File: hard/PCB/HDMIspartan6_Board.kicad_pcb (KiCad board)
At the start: 4 copper layers, 56.1 x 89.6 mm, 150 parts, among them IC1 W9812G6KH, P1 CONN_02X20, P2 CONN_01X03, U1 XC6SLX9-2TQG144C, U2 TPS62133RGTR, U3 ZLDO1117G33TA, U4 ZLDO1117G12TA, U5 MAX5864

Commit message: Add jmp Rpi Power
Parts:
- added P3: CONN_01X03, Pin_Headers:Pin_Header_Straight_1x03_Pitch2.54mm, F.Cu at (125.4, 115.0)
- added TH21, TH27, TH33, TH39: CONN_1, Project:1Pin_12mil_VIA, F.Cu at (136.3, 159.3)
- C10: value 3.3nF -> 33uF
- C4: value 33uF -> 3.3nF
- C5, C8: value 100n -> 33uF
- C6, C9: value 33uF -> 100n
- CA1, CA2, CA3, RF2, RF3: moved to F.Cu
- moved RF1 36.6 mm to (181.0, 147.4)
- moved RF4 34.7 mm to (177.4, 146.5)
- moved CF4 27.1 mm to (177.7, 142.4)
- moved CF1 26.4 mm to (177.6, 130.8)
- moved LF1 20.1 mm to (181.9, 139.7)
- moved CF3 16.9 mm to (177.7, 138.1), turned to 0 degrees
- moved RF6 16.7 mm to (182.2, 130.7), turned to 0 degrees
- moved CF6 15.1 mm to (187.3, 141.8)
- moved CF2 13.0 mm to (186.6, 130.9)
- moved CF5 12.8 mm to (182.2, 135.8), turned to 0 degrees
- moved CA2 12.7 mm to (168.7, 69.1), turned to 180 degrees
- moved CA3 11.4 mm to (168.8, 71.5), turned to 0 degrees
- moved CA1 10.9 mm to (168.6, 74.0), turned to 180 degrees
- moved PA1 10.7 mm to (162.1, 78.5), turned to 180 degrees
- moved DS2 9.36 mm to (95.1, 112.3)
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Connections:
- C10 pad 1: Net-(C10-Pad1) -> +1V2
- C4 pad 1: +5V -> Net-(C4-Pad1)
- C5 pad 1: +3V3 -> +5V
- C8 pad 1: +1V2 -> +3V3
- P1 pad 10: /spartan6/RXD -> /spartan6/TXD
- P1 pad 17: +3V3 -> Net-(P1-Pad17)
- P1 pad 2: VDD5V -> VccRpi
- P1 pad 4: VDD5V -> VccRpi
- P1 pad 8: /spartan6/TXD -> /spartan6/RXD
- U2 pad 9: Net-(C10-Pad1) -> Net-(C4-Pad1)
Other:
- board text added: "Convenciones referencias componentes: > H: HDMI. Ej.: RH1 > S: Spartan. Ej.: CS1 > A: ADC. Ej.: CA1 > F: FTDI. Ej.: RF2"

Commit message: config power
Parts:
- removed P2: CONN_01X03, Socket_Strips:Socket_Strip_Straight_1x03_Pitch2.54mm
- removed TH51, TH52, TH53, TH54: CONN_1, Project:1Pin_12mil_VIA
- C10, C5, C8: footprint Capacitors_SMD:C_0603 -> Capacitors_SMD:C_1206
- C4: footprint Capacitors_SMD:C_1206 -> Capacitors_SMD:C_0603; moved to F.Cu
- C6, C9: footprint Capacitors_SMD:C_1206 -> Capacitors_SMD:C_0603
- F1: moved to F.Cu
- P3: footprint Pin_Headers:Pin_Header_Straight_1x03_Pitch2.54mm -> Socket_Strips:Socket_Strip_Straight_1x03_Pitch2.54mm
- R1, RS1: moved to B.Cu
- moved RS1 67.0 mm to (153.5, 123.6), turned to 270 degrees
- moved TH33 59.7 mm to (77.5, 149.2)
- moved TH21 48.0 mm to (88.6, 154.1)
- moved TH27 44.8 mm to (92.7, 149.0)
- moved TH39 41.3 mm to (97.0, 146.7)
- moved S1 37.0 mm to (140.2, 152.5), turned to 0 degrees
- moved C4 20.4 mm to (123.7, 142.4)
- moved PW_LCD1 10.8 mm to (112.0, 127.4)
- moved C3 7.43 mm to (137.9, 146.4)
- moved C1 5.87 mm to (123.9, 148.0)
- moved PS1 4.59 mm to (112.5, 145.7)
- moved F1 4.27 mm to (149.6, 150.0)
- moved JMS1 3.15 mm to (160.8, 146.4)
- moved C2 2.53 mm to (126.7, 148.7)
- moved U2 1.76 mm to (128.5, 143.9)
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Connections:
- DS1 pad 1: /spartan6/LED2 -> (no net)
- DS2 pad 1: /spartan6/LED1 -> (no net)
- FT1 pad 1: Net-(FT1-Pad1) -> (no net)
- FT1 pad 11: Net-(FT1-Pad11) -> (no net)
- FT1 pad 12: Net-(FT1-Pad12) -> (no net)
- FT1 pad 13: Net-(FT1-Pad13) -> (no net)
- FT1 pad 15: Net-(FT1-Pad15) -> (no net)
- FT1 pad 16: Net-(FT1-Pad16) -> (no net)
- FT1 pad 17: Net-(FT1-Pad17) -> (no net)
- FT1 pad 19: Net-(FT1-Pad19) -> (no net)
- FT1 pad 20: Net-(FT1-Pad20) -> (no net)
- FT1 pad 27: Net-(FT1-Pad27) -> (no net)
- FT1 pad 28: Net-(FT1-Pad28) -> (no net)
- FT1 pad 29: Net-(FT1-Pad29) -> (no net)
- FT1 pad 30: Net-(FT1-Pad30) -> (no net)
- FT1 pad 32: Net-(FT1-Pad32) -> (no net)
- FT1 pad 33: Net-(FT1-Pad33) -> (no net)
- FT1 pad 35: Net-(FT1-Pad35) -> (no net)
- FT1 pad 36: Net-(FT1-Pad36) -> (no net)
- FT1 pad 37: Net-(FT1-Pad37) -> (no net)
- FT1 pad 38: Net-(FT1-Pad38) -> (no net)
- FT1 pad 41: Net-(FT1-Pad41) -> (no net)
- FT1 pad 48: Net-(FT1-Pad48) -> (no net)
- HDMI1 pad 13: Net-(HDMI1-Pad13) -> (no net)
- HDMI1 pad 14: Net-(HDMI1-Pad14) -> (no net)
- HDMI1 pad 15: Net-(HDMI1-Pad15) -> (no net)
- HDMI1 pad 16: Net-(HDMI1-Pad16) -> (no net)
- HDMI1 pad 17: Net-(HDMI1-Pad17) -> (no net)
- HDMI1 pad 18: Net-(HDMI1-Pad18) -> (no net)
- HDMI1 pad 19: Net-(HDMI1-Pad19) -> (no net)
- JMS1 pad 4: Net-(JMS1-Pad4) -> (no net)
- P1 pad 1: Net-(P1-Pad1) -> (no net)
- P1 pad 10: /spartan6/TXD -> (no net)
- P1 pad 11: Net-(P1-Pad11) -> (no net)
- P1 pad 12: Net-(P1-Pad12) -> (no net)
- P1 pad 13: Net-(P1-Pad13) -> (no net)
- P1 pad 15: Net-(P1-Pad15) -> (no net)
- P1 pad 16: Net-(P1-Pad16) -> (no net)
- P1 pad 17: Net-(P1-Pad17) -> (no net)
- P1 pad 18: Net-(P1-Pad18) -> (no net)
- P1 pad 21: /spartan6/SPI_MISO -> (no net)
- P1 pad 22: Net-(P1-Pad22) -> (no net)
- P1 pad 24: Net-(P1-Pad24) -> (no net)
- P1 pad 26: Net-(P1-Pad26) -> (no net)
- P1 pad 27: Net-(P1-Pad27) -> (no net)
- P1 pad 28: Net-(P1-Pad28) -> (no net)
- P1 pad 29: Net-(P1-Pad29) -> (no net)
- P1 pad 3: /spartan6/SDA -> (no net)
- P1 pad 31: Net-(P1-Pad31) -> (no net)
- P1 pad 32: Net-(P1-Pad32) -> (no net)
- P1 pad 33: Net-(P1-Pad33) -> (no net)
- P1 pad 35: Net-(P1-Pad35) -> (no net)
- P1 pad 36: Net-(P1-Pad36) -> (no net)
- P1 pad 37: Net-(P1-Pad37) -> (no net)
- P1 pad 38: Net-(P1-Pad38) -> (no net)
- P1 pad 40: Net-(P1-Pad40) -> (no net)
- P1 pad 5: /spartan6/SCL -> (no net)
- P1 pad 7: Net-(P1-Pad7) -> (no net)
- P1 pad 8: /spartan6/RXD -> (no net)
- PS1 pad 1: VCC -> +9V
- PS1 pad 3: Net-(PS1-Pad3) -> GND
- PW_LCD1 pad 3: Net-(PW_LCD1-Pad3) -> (no net)
- S1 pad 1: Net-(S1-Pad1) -> VDD5V
- S1 pad 2: +9V -> +5V
- S1 pad 3: VCC -> /Power/USBVCC
- U1 pad 100: Net-(U1-Pad100) -> (no net)
- U1 pad 102: Net-(U1-Pad102) -> (no net)
- U1 pad 104: Net-(U1-Pad104) -> (no net)
- U1 pad 116: Net-(U1-Pad116) -> (no net)
- U1 pad 117: Net-(U1-Pad117) -> (no net)
- U1 pad 120: Net-(U1-Pad120) -> (no net)
- U1 pad 121: Net-(U1-Pad121) -> (no net)
- U1 pad 123: Net-(U1-Pad123) -> (no net)
- U1 pad 124: Net-(U1-Pad124) -> (no net)
- U1 pad 126: Net-(U1-Pad126) -> (no net)
- U1 pad 127: Net-(U1-Pad127) -> (no net)
- U1 pad 131: Net-(U1-Pad131) -> (no net)
- U1 pad 132: Net-(U1-Pad132) -> (no net)
- U1 pad 34: Net-(U1-Pad34) -> (no net)
- U1 pad 39: Net-(U1-Pad39) -> (no net)
- U1 pad 47: Net-(U1-Pad47) -> (no net)
- U1 pad 48: Net-(U1-Pad48) -> (no net)
- U1 pad 59: Net-(U1-Pad59) -> (no net)
- U1 pad 66: Net-(U1-Pad66) -> (no net)
- U1 pad 67: Net-(U1-Pad67) -> (no net)
- U1 pad 70: Net-(U1-Pad70) -> (no net)
- U1 pad 71: Net-(U1-Pad71) -> (no net)
- U1 pad 72: Net-(U1-Pad72) -> (no net)
- U1 pad 73: Net-(U1-Pad73) -> (no net)
- U1 pad 74: Net-(U1-Pad74) -> (no net)
- U1 pad 75: Net-(U1-Pad75) -> (no net)
- U1 pad 78: Net-(U1-Pad78) -> (no net)
- U1 pad 79: Net-(U1-Pad79) -> (no net)
- U1 pad 80: Net-(U1-Pad80) -> (no net)
- U1 pad 81: Net-(U1-Pad81) -> (no net)
- U1 pad 82: Net-(U1-Pad82) -> (no net)
- U1 pad 83: Net-(U1-Pad83) -> (no net)
- U1 pad 84: Net-(U1-Pad84) -> (no net)
- U1 pad 85: Net-(U1-Pad85) -> (no net)
- U1 pad 87: Net-(U1-Pad87) -> (no net)
- U1 pad 88: Net-(U1-Pad88) -> (no net)
- U1 pad 92: Net-(U1-Pad92) -> (no net)
- U1 pad 93: Net-(U1-Pad93) -> (no net)
- U1 pad 95: Net-(U1-Pad95) -> (no net)
- U1 pad 97: Net-(U1-Pad97) -> (no net)
- U1 pad 98: Net-(U1-Pad98) -> (no net)
- U1 pad 99: Net-(U1-Pad99) -> (no net)
- U5 pad 13: /ADC_DAC/DA0 -> (no net)
- U5 pad 14: /ADC_DAC/DA1 -> (no net)
- U5 pad 15: /ADC_DAC/DA2 -> (no net)
- U5 pad 16: /ADC_DAC/DA3 -> (no net)
- U5 pad 19: /ADC_DAC/DA4 -> (no net)
- U5 pad 20: /ADC_DAC/DA5 -> (no net)
- U5 pad 21: /ADC_DAC/DA6 -> (no net)
- U5 pad 22: /ADC_DAC/DA7 -> (no net)
- U5 pad 23: /ADC_DAC/DD0 -> (no net)
- U5 pad 24: /ADC_DAC/DD1 -> (no net)
- U5 pad 25: /ADC_DAC/DD2 -> (no net)
- U5 pad 26: /ADC_DAC/DD3 -> (no net)
- U5 pad 27: /ADC_DAC/DD4 -> (no net)
- U5 pad 28: /ADC_DAC/DD5 -> (no net)
- U5 pad 29: /ADC_DAC/DD6 -> (no net)
- U5 pad 30: /ADC_DAC/DD7 -> (no net)
- U5 pad 31: /ADC_DAC/DD8 -> (no net)
- U5 pad 32: /ADC_DAC/DD9 -> (no net)
- U5 pad 36: /ADC_DAC/CS_AD -> (no net)
- U5 pad 38: Net-(U5-Pad38) -> (no net)
- U5 pad 7: Net-(U5-Pad7) -> (no net)
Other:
- board size 56.1 x 89.6 mm -> 56.1 x 95.3 mm
- net class Vcc added: clearance 0.5, trace_width 0.4, via_dia 1, via_drill 0.6

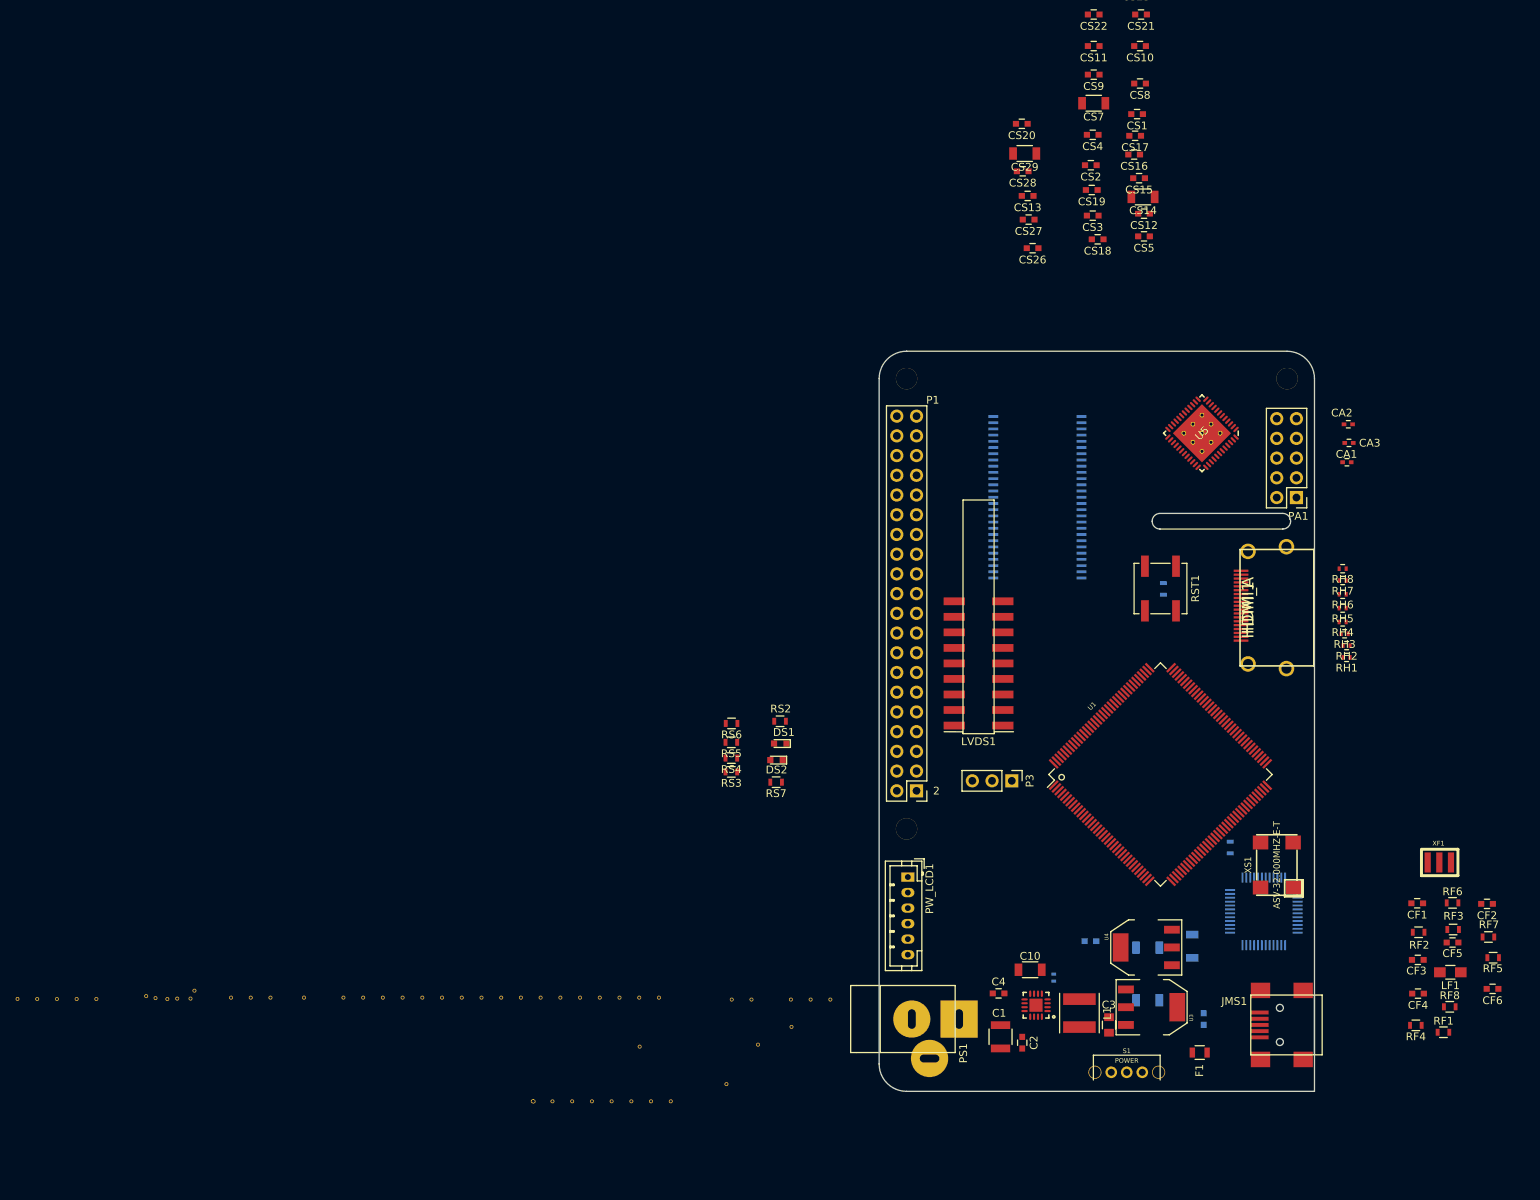
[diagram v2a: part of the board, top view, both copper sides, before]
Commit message: se modifican el pin hdmi- las resitencias RN1 - eñ conector de  voltaje
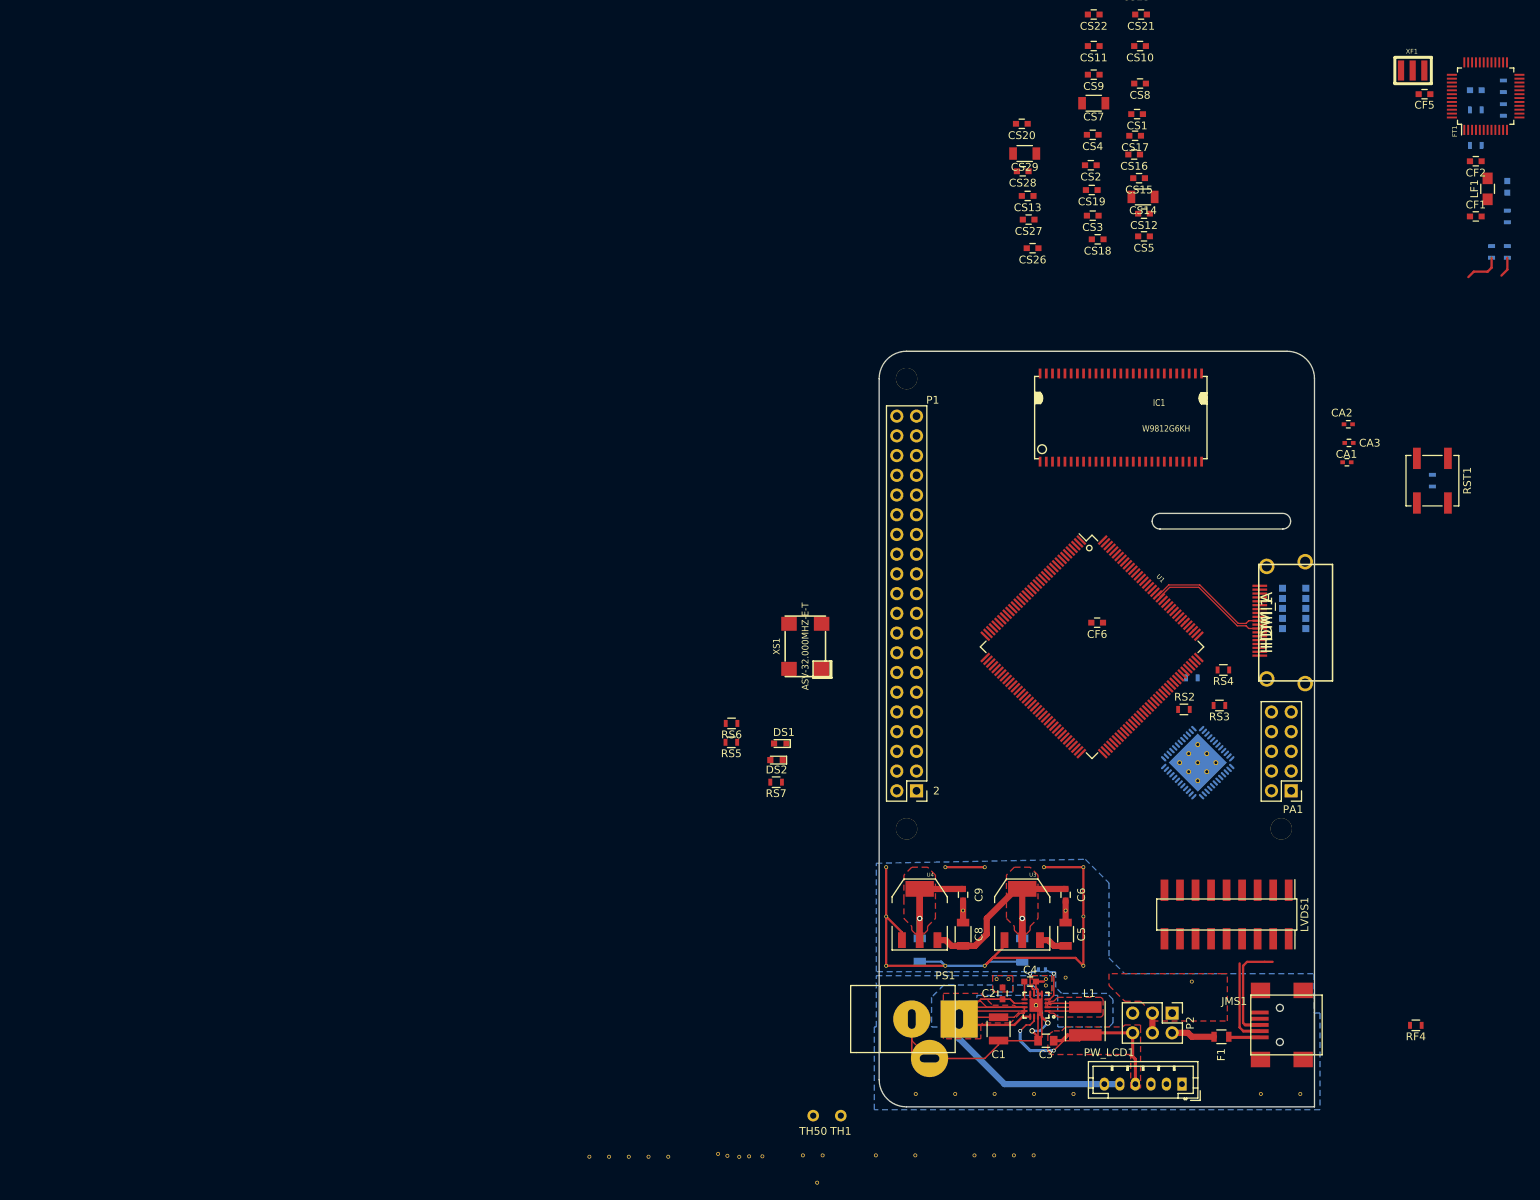
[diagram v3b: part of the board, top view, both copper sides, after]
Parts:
- removed the ? at (160.9, 63.2)
- removed the ? at (111.8, 121.2)
- removed P3: CONN_01X03, Socket_Strips:Socket_Strip_Straight_1x03_Pitch2.54mm
- removed RH1, RH2, RH3, RH4, RH5, RH6, RH7, RH8: 51, Resistors_SMD:R_0402
- removed S1: POWER, Project:CKCOMP-OS102011MA1QN1
- added ?: , Project:RPi_Hat_Mounting_Hole, F.Cu at (160.1, 121.2)
- added ?: , Project:RPi_Hat_Mounting_Hole, F.Cu at (111.8, 121.2)
- added P2: CONN_02X03, Pin_Headers:Pin_Header_Straight_2x03_Pitch2.54mm, F.Cu at (146.0, 144.9)
- added RN1: Resistors_array_8, Resistors_SMD:R_Array_Convex_5x1206, B.Cu at (161.8, 92.8)
- C10, CF3, CF4, RF1, RF2, RF3, RF5, RF6, RF7, RF8, U5: moved to B.Cu
- C5, C6, C8, C9, FT1, IC1: moved to F.Cu
- TH1, TH50: footprint Project:1Pin_12mil_VIA -> Measurement_Points:Measurement_Point_Round-TH_Small
- moved RF1 118.9 mm to (185.2, 28.6)
- moved RF8 118.8 mm to (188.7, 25.5), turned to 270 degrees
- moved CF3 112.3 mm to (185.2, 26.1)
- moved CF5 109.3 mm to (178.6, 26.6)
- moved FT1 108.8 mm to (186.4, 26.8)
- moved CF4 104.5 mm to (189.2, 38.5), turned to 90 degrees
- moved RF6 102.3 mm to (188.7, 28.6), turned to 90 degrees
- moved XF1 102.1 mm to (177.0, 23.5)
- moved RF7 102.0 mm to (185.2, 33.2)
- moved LF1 101.0 mm to (186.7, 38.8), turned to 90 degrees
- moved CF2 95.7 mm to (185.2, 35.2)
- moved RF5 95.5 mm to (189.2, 42.3), turned to 270 degrees
- moved CF1 88.8 mm to (185.2, 42.3), turned to 0 degrees
- moved RF2 88.1 mm to (187.2, 46.9), turned to 270 degrees
- moved RF3 87.6 mm to (189.2, 46.9), turned to 270 degrees
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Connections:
- CF1 pad 1: /Power/USBVCC -> +5V
- LF1 pad 1: /Power/USBVCC -> +5V
- U1 pad 111: /spartan6/TMDS_D2_N -> /spartan6/TMDS_D0_N
- U1 pad 112: /spartan6/TMDS_D2_P -> /spartan6/TMDS_D0_P
- U1 pad 116: (no net) -> /spartan6/TMDS_D2_N
- U1 pad 117: (no net) -> /spartan6/TMDS_D2_P
- U1 pad 118: /spartan6/TMDS_D0_N -> (no net)
- U1 pad 119: /spartan6/TMDS_D0_P -> (no net)
- U1 pad 123: (no net) -> /spartan6/TMDS_CLK_N
- U1 pad 124: (no net) -> /spartan6/TMDS_CLK_P
- U1 pad 133: /spartan6/TMDS_CLK_N -> (no net)
- U1 pad 134: /spartan6/TMDS_CLK_P -> (no net)
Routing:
- net GND: track 0.00 -> 143.1 mm, vias 0 -> 3
- net +9V: track 0.00 -> 92.7 mm
- net VDD5V: track 0.00 -> 35.6 mm, vias 0 -> 2
- net +3V3: track 0.00 -> 33.0 mm, vias 0 -> 1
- net +1V2: track 0.00 -> 18.6 mm, vias 0 -> 1
- net Net-(L1-Pad2): track 0.00 -> 16.0 mm
- net /spartan6/TMDS_CLK_P: track 0.00 -> 15.9 mm
- net /spartan6/TMDS_CLK_N: track 0.00 -> 15.6 mm
- net Net-(JMS1-Pad3): track 0.00 -> 15.5 mm
- net Net-(JMS1-Pad2): track 0.00 -> 11.0 mm
- net (no net): track 0.00 -> 7.69 mm
- net +5V: track 0.00 -> 6.15 mm
- net /Power/USBVCC: track 0.00 -> 5.61 mm
- net /Power/PG: track 0.00 -> 5.00 mm, vias 0 -> 1
- net Net-(F1-Pad2): track 0.00 -> 4.01 mm
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- added copper zone on F.Cu, net +1V2
- added copper zone on F.Cu, net +3V3
- added copper zone on F.Cu, net +9V
- added copper zone on B.Cu, net GND
- added copper zone on F.Cu, net GND
- added copper zone on F.Cu, net Net-(L1-Pad2)
- added copper zone on F.Cu, net VDD5V
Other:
- board size 56.1 x 95.3 mm -> 56.1 x 97.3 mm
- copper layers 4 -> 2
- net class Default: trace_width 0.1 -> 0.3
- net class Vcc: clearance 0.5 -> 0.2; trace_width 0.4 -> 0.3; via_dia 1 -> 0.7; via_drill 0.6 -> 0.4
- rule via_min_drill: 0.2 -> 0.3
